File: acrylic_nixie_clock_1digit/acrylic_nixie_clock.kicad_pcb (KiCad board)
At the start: 2 copper layers, 33 x 33 mm, 28 parts, among them J1 AVR-ISP-6, SW1 SW_Push, U1 ATtiny13A-SSU, U2 TPS61041DDC

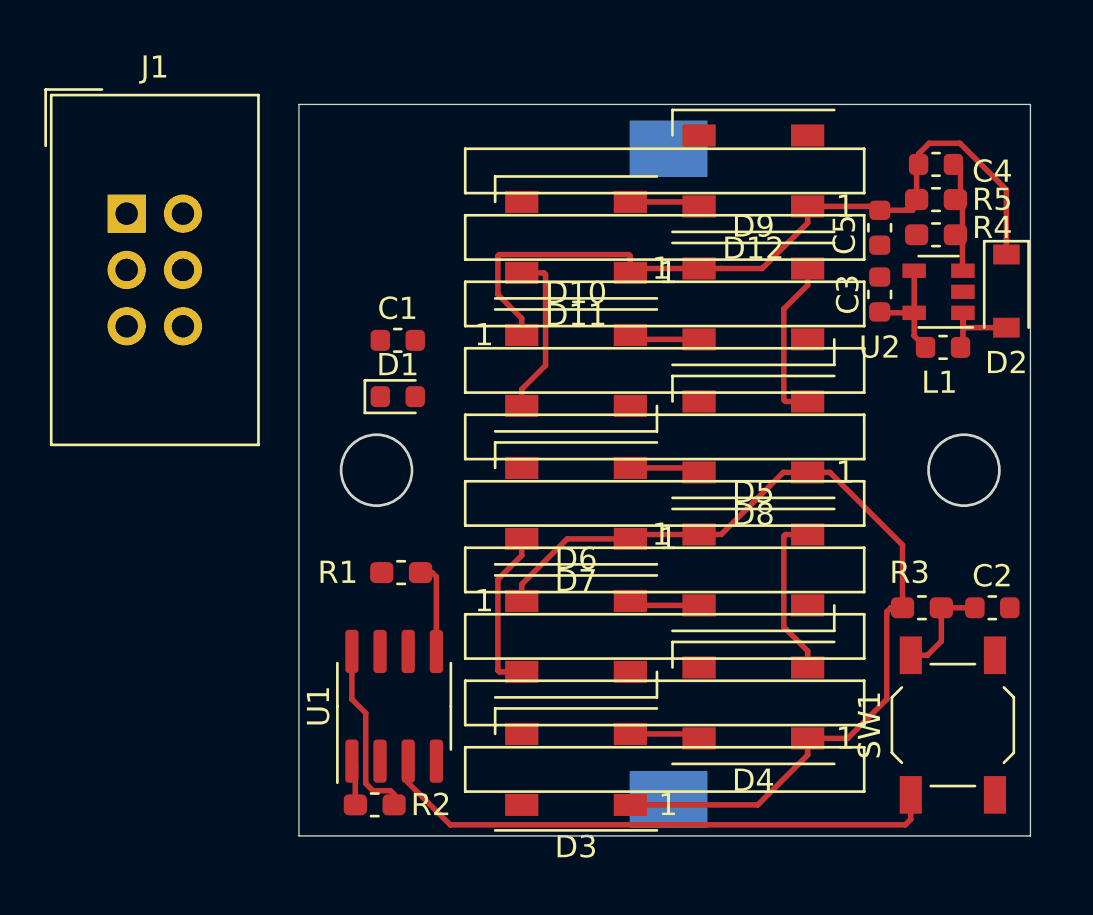
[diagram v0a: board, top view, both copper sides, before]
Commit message: 問題点を修正
CH304Gの電源電圧を3.3Vに
RSTにコンデンサを追加
USBのフットプリントを修正
カードコネクタの追加
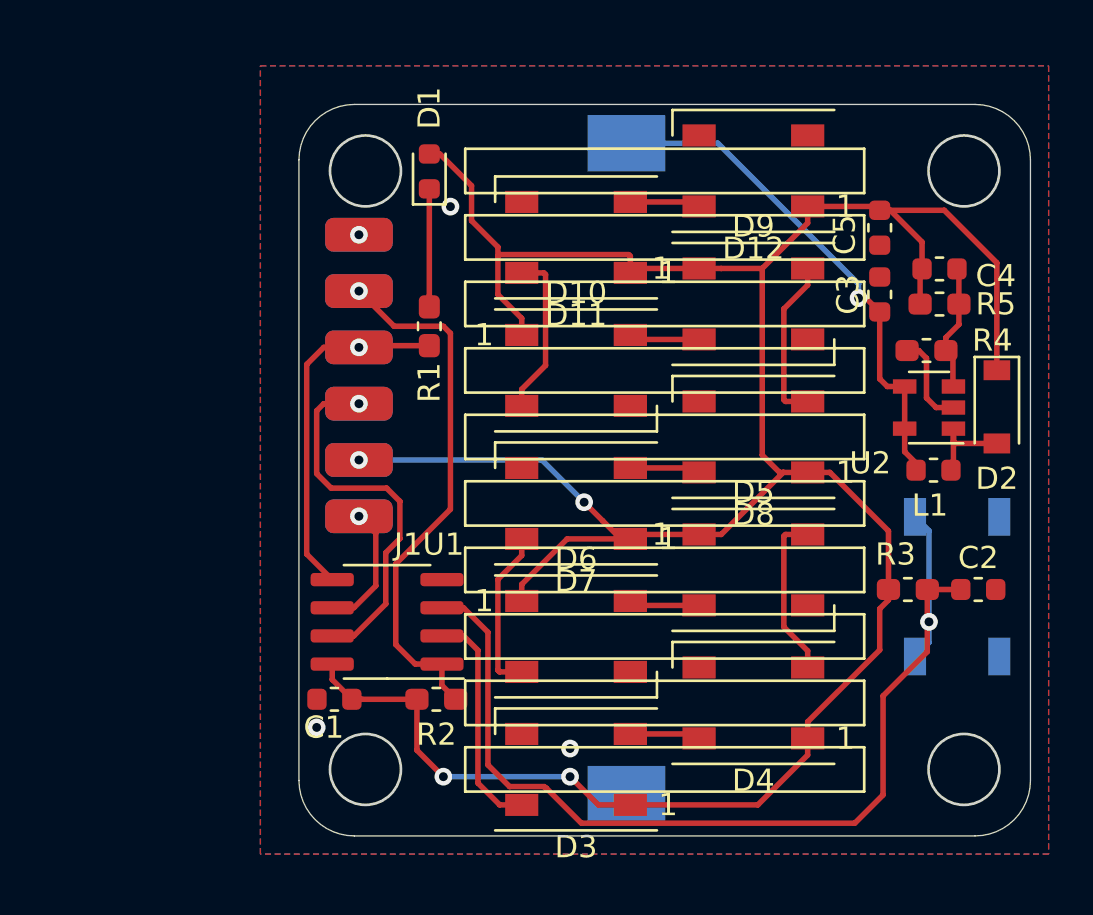
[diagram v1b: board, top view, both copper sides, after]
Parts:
- J1: footprint Connector_IDC:IDC-Header_2x03_P2.54mm_Vertical -> acrylic_nixie_clock_1digit:ISP-6
- SW1: moved to B.Cu
- moved J1 19.3 mm to (52.7, 71.1), turned to 180 degrees
- moved C1 16.4 mm to (51.6, 76.8), turned to 180 degrees
- moved R1 11.2 mm to (55.9, 60.0), turned to 270 degrees
- moved D1 10.3 mm to (55.9, 53.0), turned to 90 degrees
- moved SW1 6.25 mm to (79.7, 71.8), turned to 270 degrees
- moved L1 5.56 mm to (78.6, 66.5)
- moved R2 5.51 mm to (56.2, 76.8), turned to 180 degrees
- moved D2 5.24 mm to (81.5, 63.6)
- moved U2 5.24 mm to (78.4, 63.7)
- moved R4 5.24 mm to (78.3, 61.1)
- moved C4 4.72 mm to (78.9, 57.4)
- moved R5 4.72 mm to (78.9, 59.0)
- moved U1 3.82 mm to (54.0, 73.3), turned to 180 degrees
- moved BT1 1.92 mm to (64.8, 66.4)
- moved C2 1.04 mm to (80.6, 71.9)
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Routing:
- net +5V: track 87.4 -> 128.5 mm, vias 0 -> 4
- net RST: track 2.03 -> 24.3 mm, vias 0 -> 1
- net Net-(BT1-Pad1): track 5.24 -> 22.5 mm, vias 0 -> 1
- net SCK: track 0.00 -> 17.1 mm, vias 0 -> 1
- net SW: track 30.3 -> 46.7 mm, vias 0 -> 1
- net MOSI: track 4.16 -> 16.1 mm, vias 0 -> 1
- net DIN: track 0.00 -> 10.3 mm
- net MISO: track 0.00 -> 5.83 mm, vias 0 -> 1
- net Net-(D1-Pad1): track 0.00 -> 5.32 mm
- net GND: track 0.00 -> 4.20 mm, vias 0 -> 4
- net Net-(C4-Pad2): track 4.84 -> 5.59 mm
- added copper zone on B.Cu, net GND
- added copper zone on F.Cu, net GND
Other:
- outline, holes or cut-outs redrawn
